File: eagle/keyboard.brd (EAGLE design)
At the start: 100 x 100 mm, 72 parts, among them IC1 STC12C5616AD, Q1 12MHz

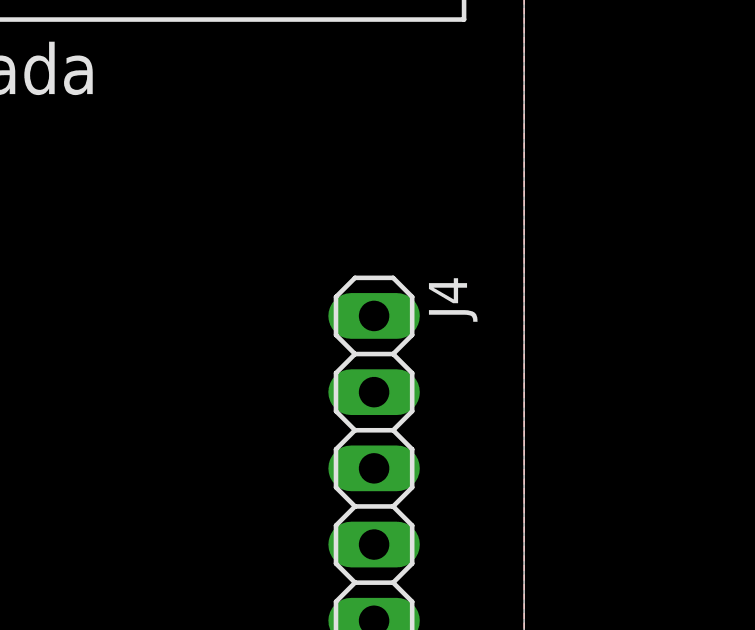
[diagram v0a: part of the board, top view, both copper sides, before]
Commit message: Finish keyboard PCB
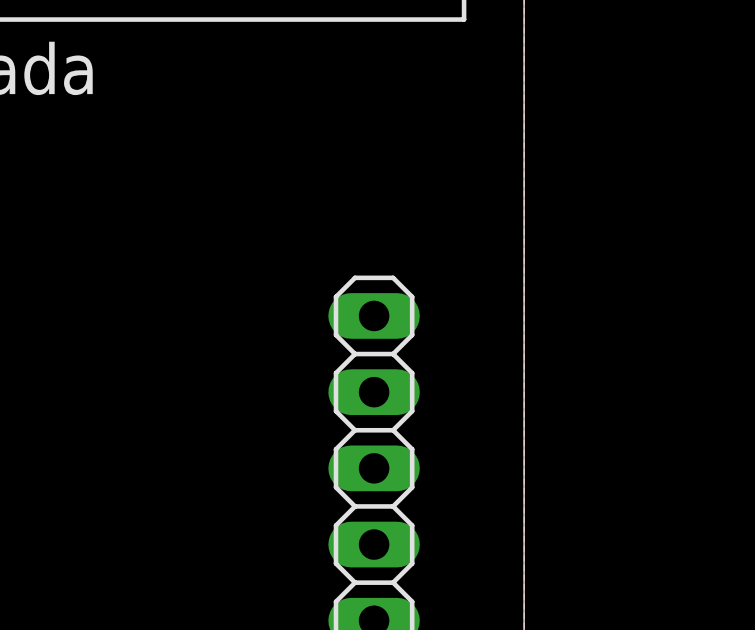
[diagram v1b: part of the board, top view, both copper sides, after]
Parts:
- J4: value (none) -> RESERVED
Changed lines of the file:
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@@
 <drawing>
 <settings>
-<setting alwaysvectorfont="no"/>
+<setting alwaysvectorfont="yes"/>
 <setting verticaltext="up"/>
 </settings>
@@
 <attribute name="VALUE" x="113.161" y="78" size="1.27" layer="27" rot="R90" align="top-center"/>
 </element>
-<element name="J4" library="pinhead" library_urn="urn:adsk.eagle:library:325" package="1X07" package3d_urn="urn:adsk.eagle:package:22477/2" value="" x="155" y="77" smashed="yes" rot="R270">
-<attribute name="NAME" x="156.8288" y="85.9662" size="1.27" layer="25" ratio="10" rot="R270"/>
-<attribute name="VALUE" x="151.825" y="85.89" size="1.27" layer="27" rot="R270"/>
+<element name="J4" library="pinhead" library_urn="urn:adsk.eagle:library:325" package="1X07" package3d_urn="urn:adsk.eagle:package:22477/2" value="RESERVED" x="155" y="77" smashed="yes" rot="R270">
+<attribute name="VALUE" x="156.825" y="85.39" size="1.27" layer="27" rot="R270"/>
 </element>
 </elements>

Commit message: Finish basic component placement
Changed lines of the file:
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@@
 <drawing>
 <settings>
-<setting alwaysvectorfont="yes"/>
+<setting alwaysvectorfont="no"/>
 <setting verticaltext="up"/>
 </settings>
@@
 <contactref element="J1" pad="1"/>
 <contactref element="J1" pad="2"/>
-<wire x1="66.92" y1="95.397" x2="67" y2="95.317" width="0.1524" layer="1"/>
 <wire x1="63" y1="75.81" x2="63" y2="85" width="0.3" layer="1"/>
 <wire x1="101" y1="96.81" x2="104" y2="96.81" width="0.3" layer="1"/>
